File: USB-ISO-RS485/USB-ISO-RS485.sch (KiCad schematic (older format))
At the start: 35 parts, among them P1 CONN_01X03, P2 USB_A, U1 ADM2582E, U2 FT232RL

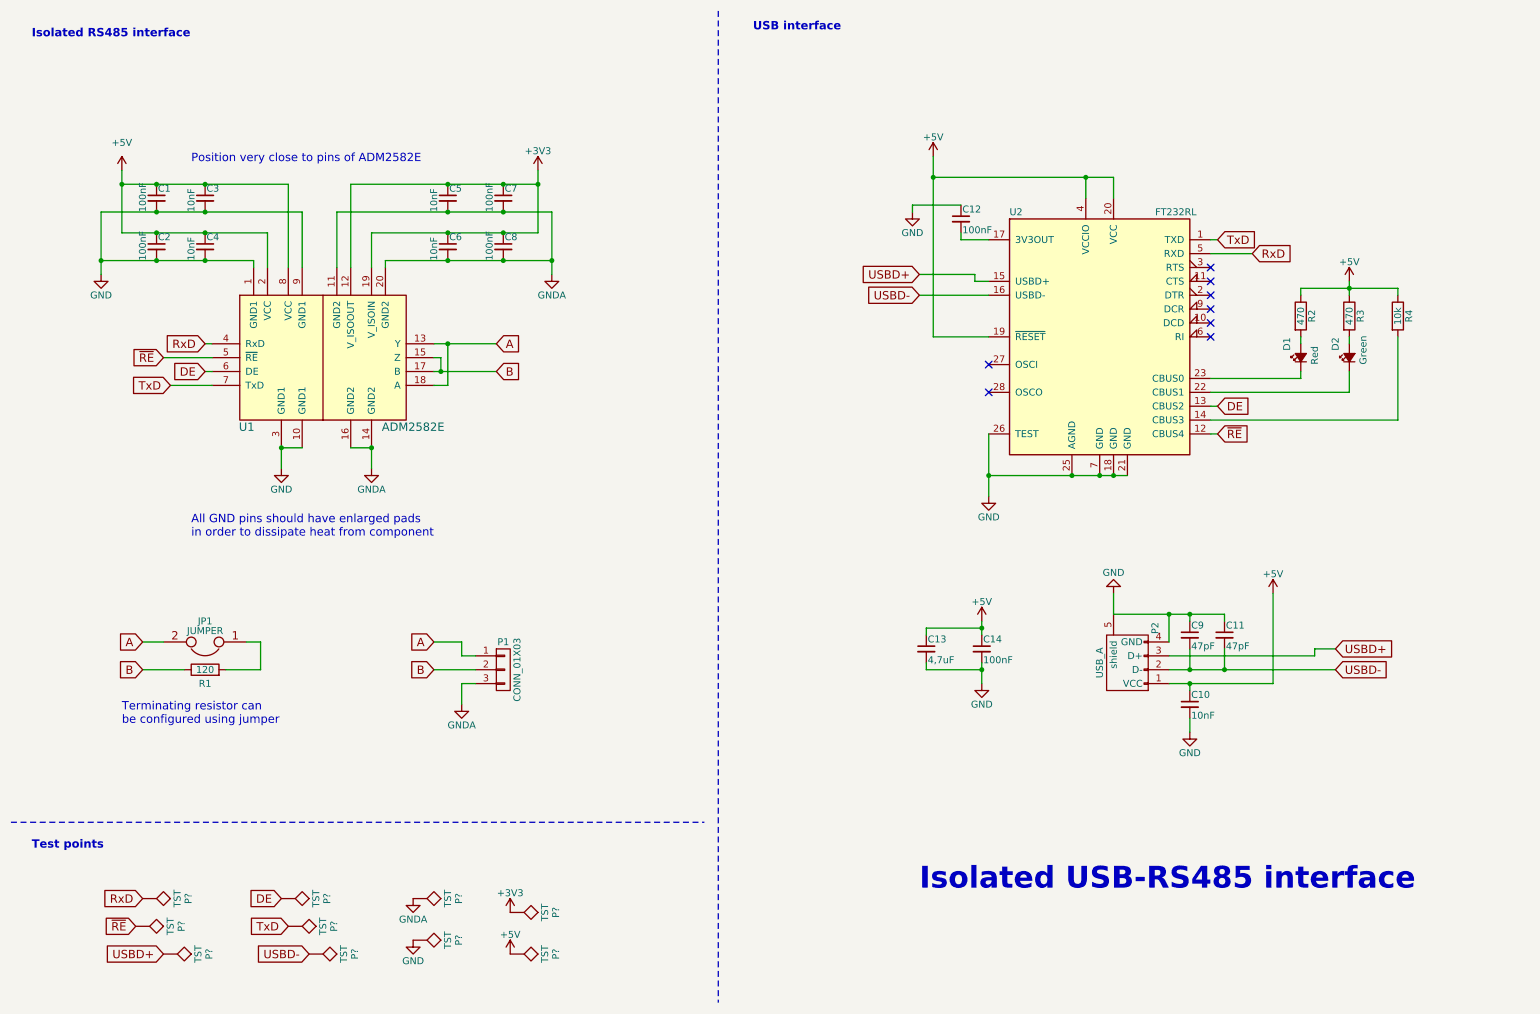
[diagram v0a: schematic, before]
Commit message: Added UART interface header, exported schematic as PDF
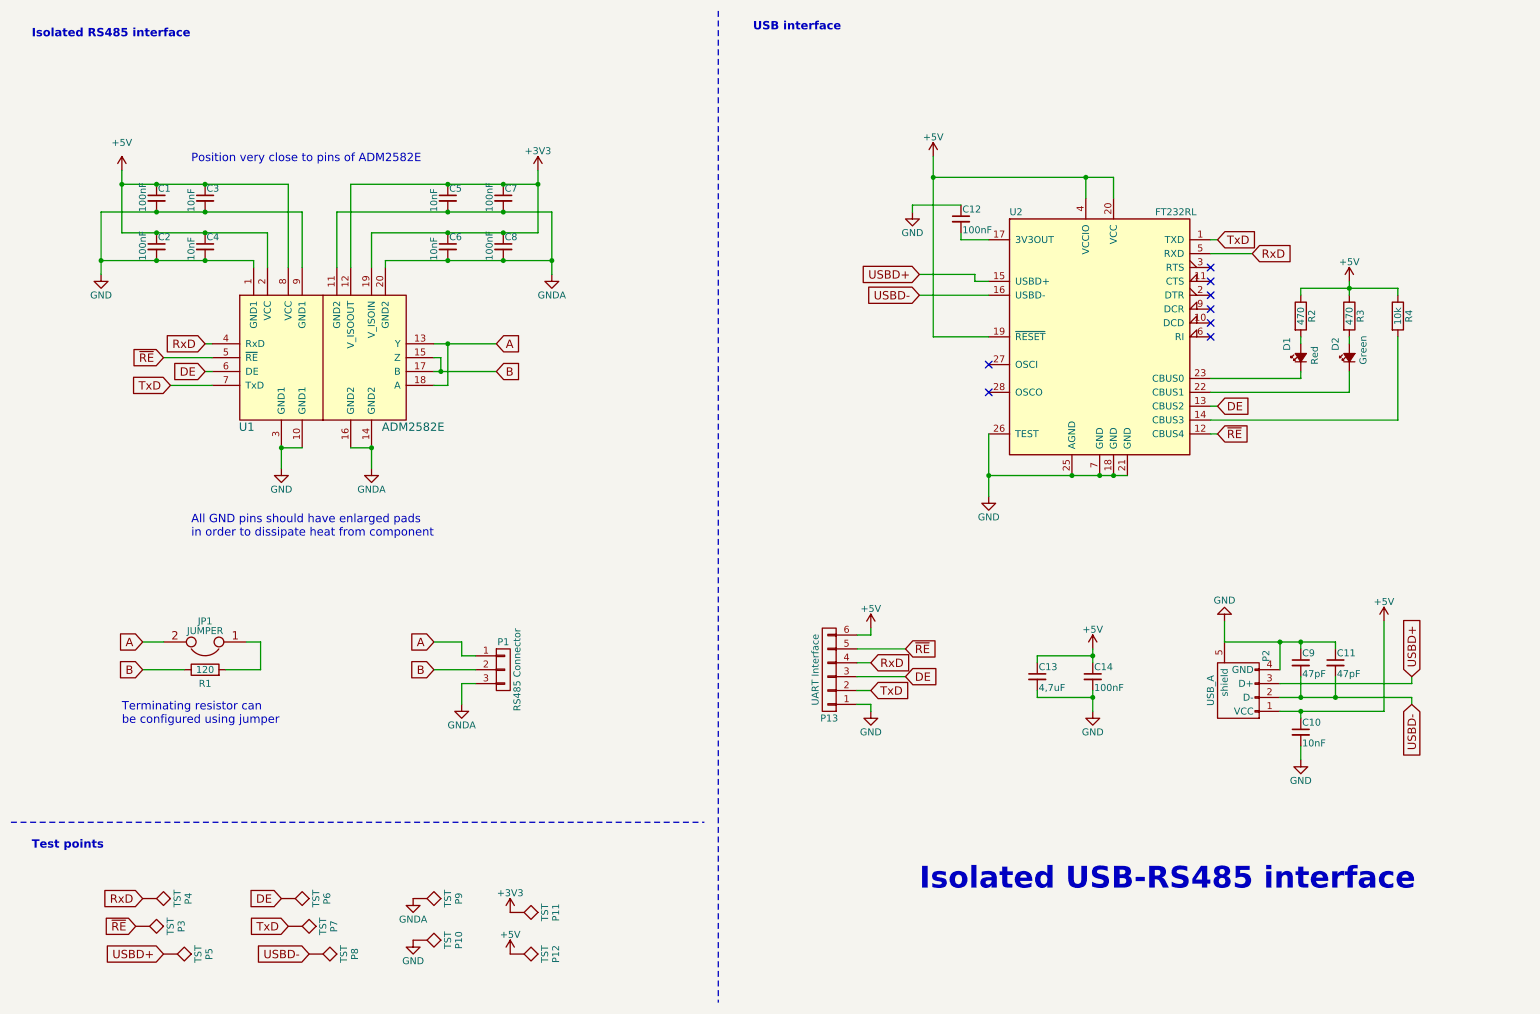
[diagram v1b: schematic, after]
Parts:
- added P13: UART Interface, symbol CONN_01X06
- P1: value CONN_01X03 -> RS485 Connector
- gave numbers to parts that had none: 10
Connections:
- net +5V: now also P13.6 (P6)
- net DE: now also P13.3 (P3)
- net GND: now also P13.1 (P1)
- net RxD: now also P13.4 (P4)
- net TxD: now also P13.2 (P2)
- net ~RE: now also P13.5 (P5)
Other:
- moved on the sheet: C10, C11, C13, C14, C9, P2
